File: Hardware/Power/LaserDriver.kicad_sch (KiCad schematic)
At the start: 99 parts, among them Q1 PSMN1R5-25MLHX, Q2 PSMN1R5-25MLHX, Q3 PSMN1R5-25MLHX, Q4 PSMN1R5-25MLHX, Q5 PSMN1R5-25MLHX, Q6 PSMN1R5-25MLHX, Q7 PSMN1R5-25MLHX, Q8 PSMN1R5-25MLHX, U2 TMP390-Q1, U3 SN74LVC1G08DCK3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

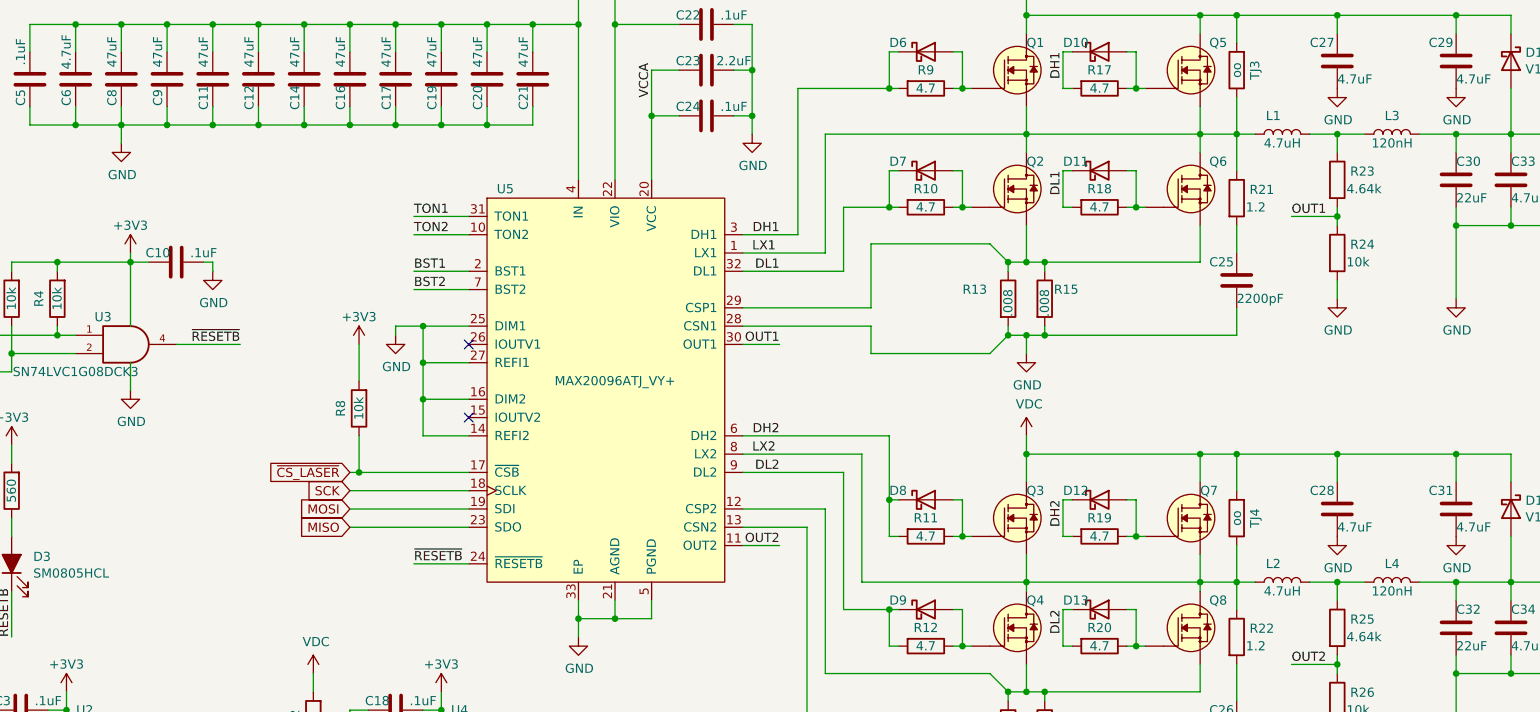
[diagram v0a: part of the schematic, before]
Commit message: Update to kicad 8
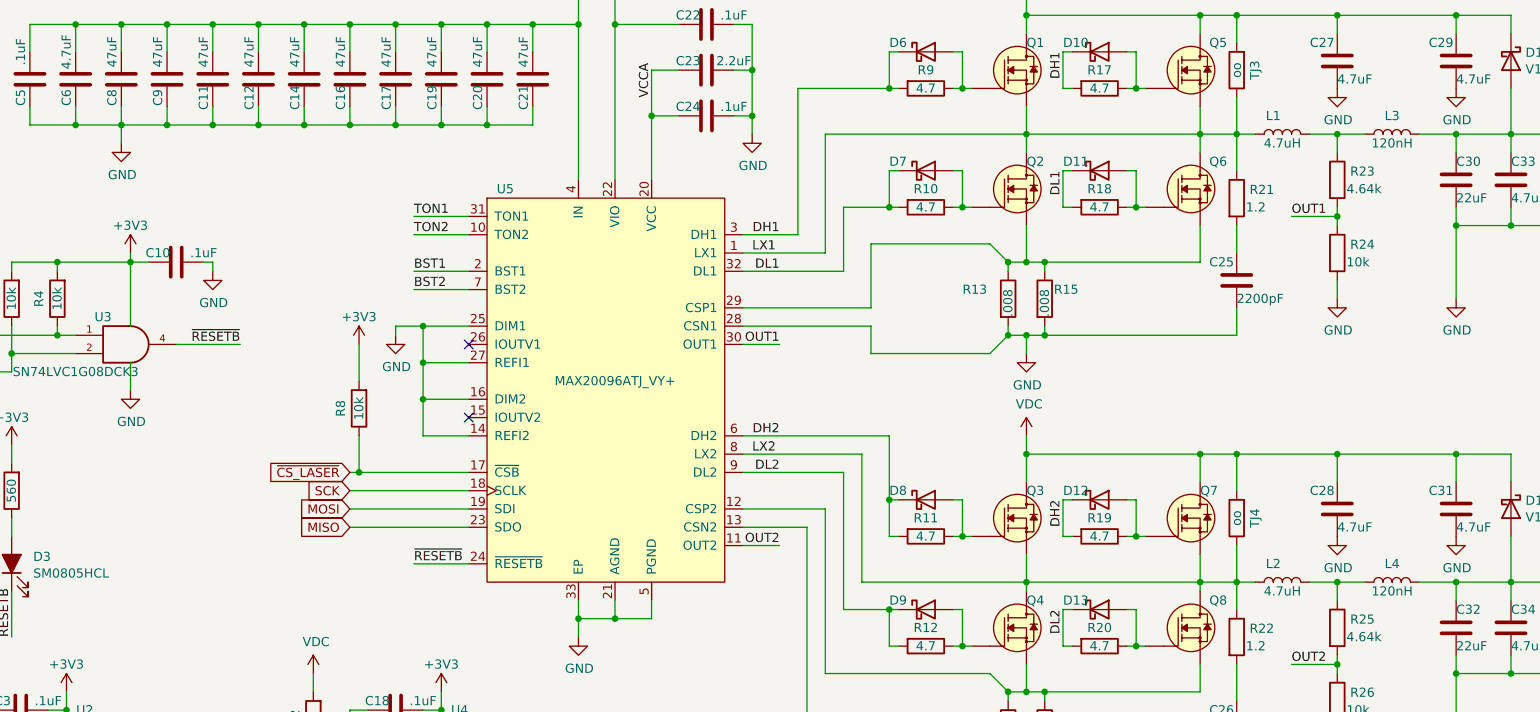
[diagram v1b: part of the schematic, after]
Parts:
- D3: footprint LED_SMD:LED_0805_2012Metric_Castellated -> LED_SMD:LED_0805_2012Metric
